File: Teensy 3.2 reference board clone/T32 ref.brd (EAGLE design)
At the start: 71.1 x 25.4 mm, 89 parts, among them K1 MK20DX256VLH7, K2 MKL04Z32VLC4, T1 MCP1825S, X1 MINI-USB

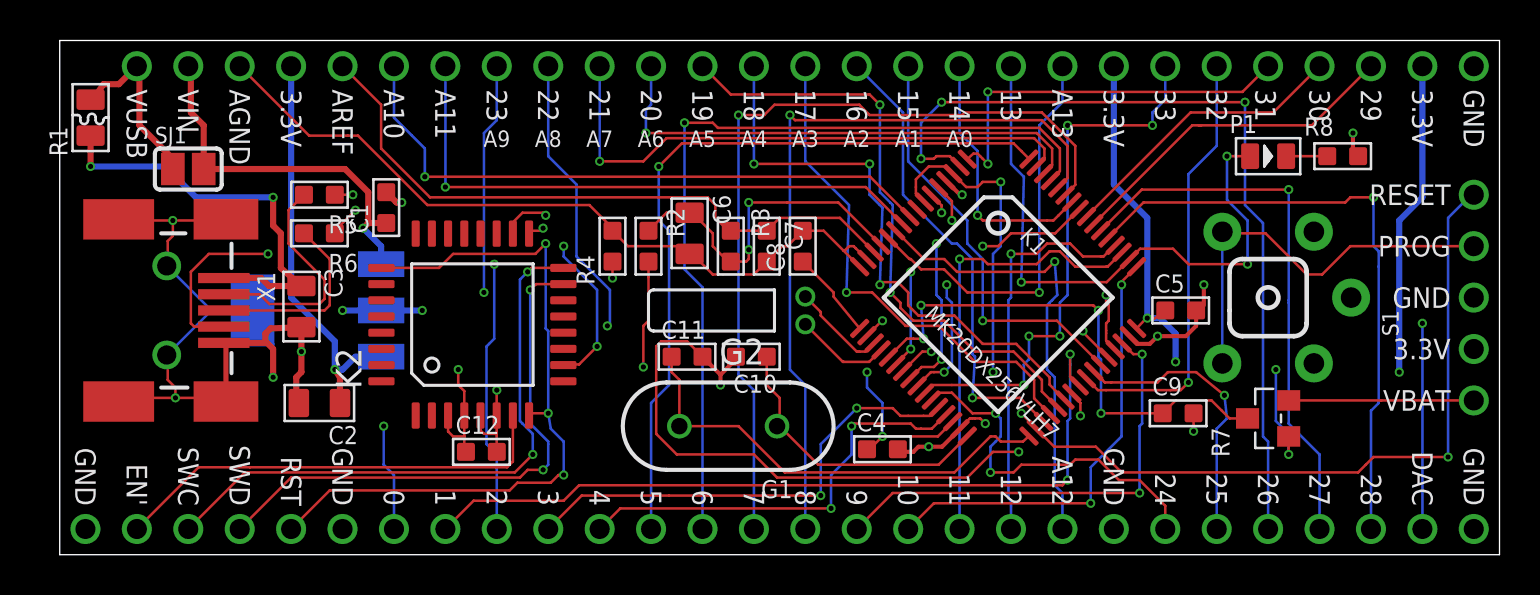
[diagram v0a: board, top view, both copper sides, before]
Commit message: improved silkscreen improved usb mini footprint new ground plane below the voltage regulator
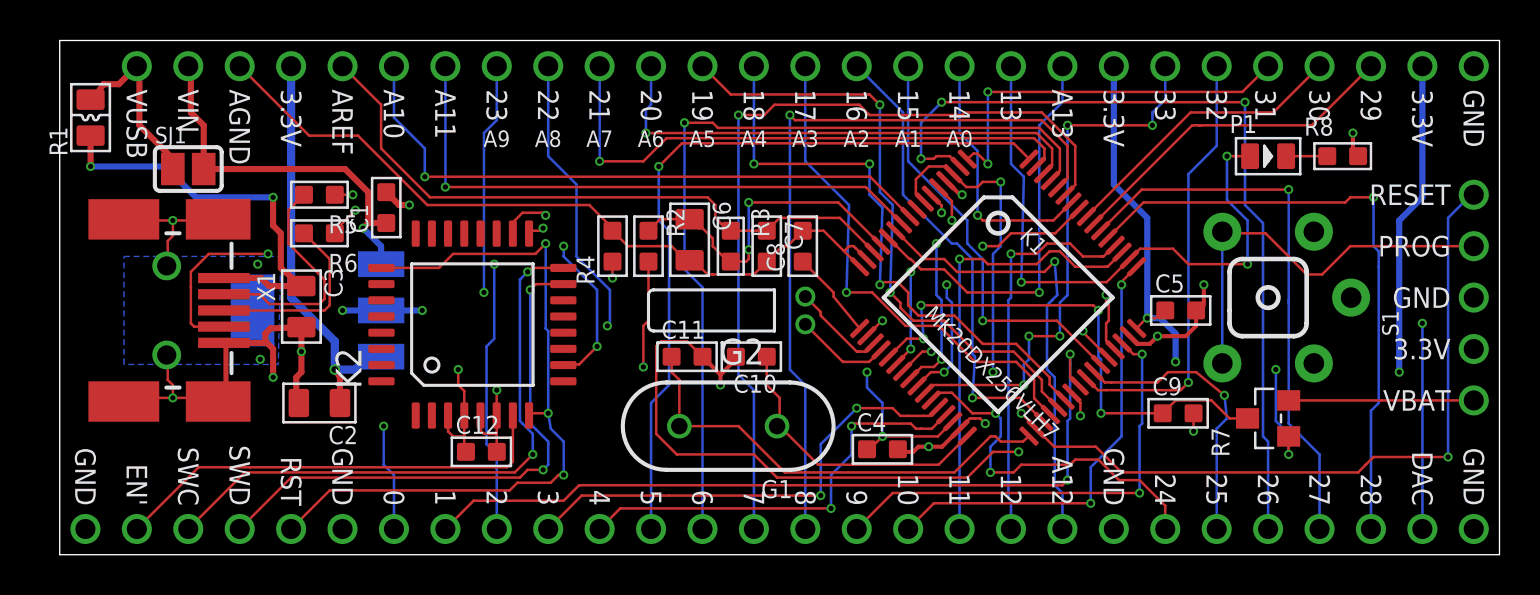
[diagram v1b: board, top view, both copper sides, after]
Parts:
- moved C6 0.32 mm to (31.1, 15.6)
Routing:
- net GND: track 95.3 -> 88.0 mm, vias 18 -> 20
- added copper zone on layer 16, net GND
